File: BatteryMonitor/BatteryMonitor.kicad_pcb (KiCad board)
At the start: 4 copper layers, 40 x 40 mm, 62 parts, among them J1 SWD, J2 BAT+, J3 BAL_THERM, J4 I2C, J5 BAT-, J6 PACK_OUT, J7 PWR_SWITCH, Q1 NTMFS0D6N04XM, Q2 NTMFS0D6N04XM, SW1 WAKE, U1 BQ76905, U2 STM32L071KZUx

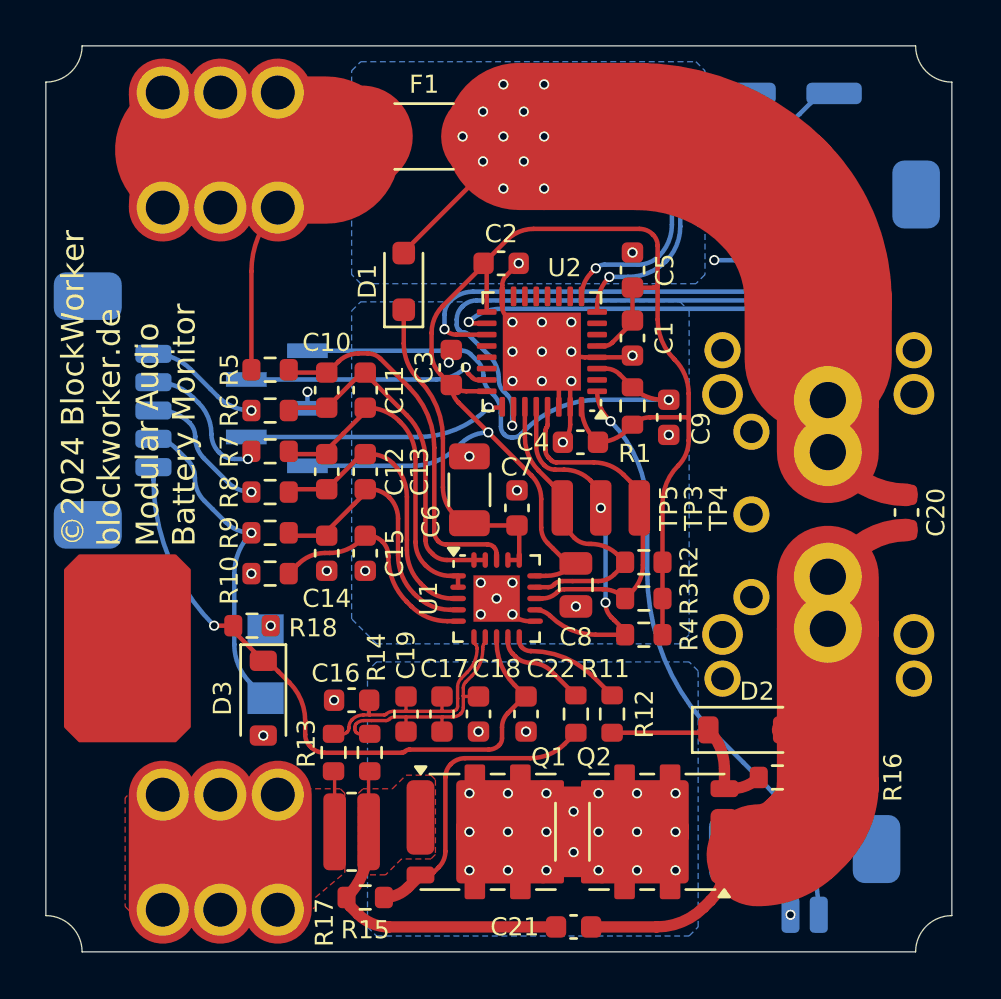
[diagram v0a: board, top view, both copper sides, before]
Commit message: BatteryMonitor v1.1: I2C swap, isolation
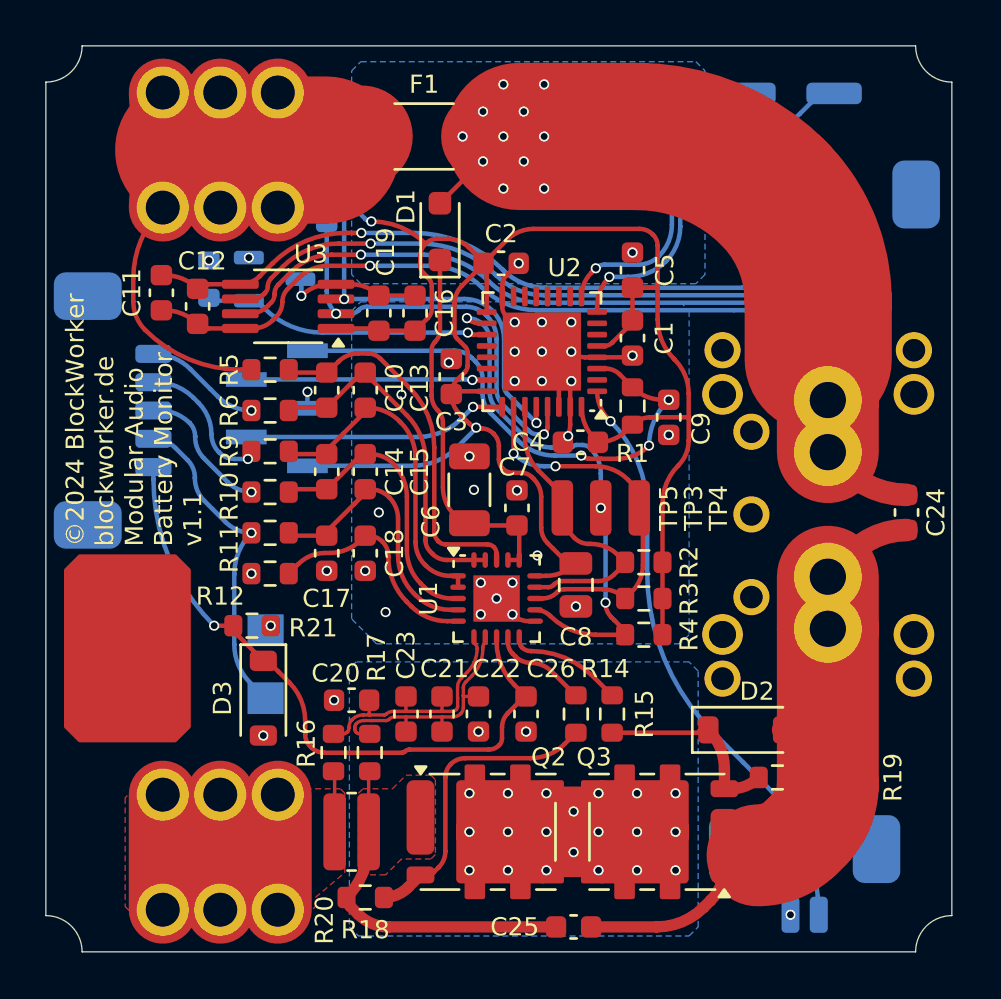
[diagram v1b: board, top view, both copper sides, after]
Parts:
- added C11: 0.1µF, Capacitor_SMD:C_0603_1608Metric, F.Cu at (135.1, 90.9)
- added C12: 1nF, Capacitor_SMD:C_0603_1608Metric, F.Cu at (136.7, 91.5)
- added C16: 0.1µF, Capacitor_SMD:C_0603_1608Metric, F.Cu at (146.3, 91.8)
- added C19: 1nF, Capacitor_SMD:C_0603_1608Metric, F.Cu at (144.7, 91.8)
- added Q1: NX138BK, Package_TO_SOT_SMD:SOT-23-3, B.Cu at (140.1, 90.3)
- added R13: 1MΩ, Resistor_SMD:R_0603_1608Metric, B.Cu at (137.2, 90.3)
- added R7: 10kΩ, Resistor_SMD:R_0603_1608Metric, B.Cu at (142.4, 83.9)
- added R8: 10kΩ, Resistor_SMD:R_0603_1608Metric, B.Cu at (142.4, 87.0)
- added U3: ADuM1252, Package_SO:MSOP-8_3x3mm_P0.65mm, F.Cu at (140.7, 91.5)
- moved D1 2.72 mm to (147.4, 88.2)
- moved C3 0.40 mm to (147.9, 94.6)
- renumbered C11 to C13, C12 to C14, C13 to C15, C14 to C17, C15 to C18, C16 to C20, C17 to C21, C18 to C22, C19 to C23, C20 to C24, C21 to C25, C22 to C26, Q1 to Q2, Q2 to Q3, R8 to R10, R9 to R11, R10 to R12, R11 to R14, R12 to R15, R13 to R16, R14 to R17, R15 to R18, R16 to R19, R17 to R20, R18 to R21, R7 to R9
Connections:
- J4 pad 2: /SDA_EXT -> Net-(J4-Pin_2)
- J4 pad 4: GND -> GNDEXT
- R4 pad 2: Net-(U1-SCL) -> /SCL_BMS
- TP4 pad 1: Net-(U1-SCL) -> /SCL_BMS
- U1 pad 12: Net-(U1-SCL) -> /SCL_BMS
- U2 pad 18: Net-(J4-Pin_1) -> /SCL_BMS
- U2 pad 19: Net-(J4-Pin_3) -> Net-(Q1-G)
- U2 pad 26: /SDA_EXT -> Net-(U1-SDA)
- U2 pad 28: Net-(U1-SCL) -> /SCL_ISO
- U2 pad 29: Net-(U1-SDA) -> /SDA_ISO
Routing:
- net GNDEXT: track 0.00 -> 29.1 mm, vias 0 -> 1
- net Net-(J4-Pin_2): track 0.00 -> 28.5 mm, vias 0 -> 1
- net /SDA_EXT: track 24.4 -> 0.00 mm, vias 1 -> 0
- net /SCL_BMS: track 0.00 -> 23.5 mm, vias 0 -> 3
- net +3.3V: track 68.0 -> 90.9 mm, vias 1 -> 2
- net /SCL_ISO: track 0.00 -> 20.2 mm, vias 0 -> 2
- net /SDA_ISO: track 0.00 -> 18.7 mm, vias 0 -> 2
- net Net-(U1-SCL): track 16.4 -> 0.00 mm, vias 2 -> 0
- net Net-(J4-Pin_1): track 19.3 -> 33.7 mm
- net Net-(Q1-G): track 0.00 -> 12.7 mm, vias 0 -> 1
- net Net-(J4-Pin_3): track 19.7 -> 27.1 mm
- net Net-(Q1-D): track 0.00 -> 6.02 mm, vias 0 -> 1
- net GND: track 34.2 -> 30.9 mm, vias 33 -> 39
- net +BATT: track 36.7 -> 34.1 mm
- net Net-(J2-Pin_1): track 33.7 -> 35.9 mm
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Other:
- board text added: "I^{2}C/UART"
- board text added: "Modular Audio Battery Monitor v1.1"
- board text removed: "I^{2}C"
- board text removed: "Modular Audio Battery Monitor"
